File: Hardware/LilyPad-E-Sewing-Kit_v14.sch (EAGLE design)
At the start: 43 parts

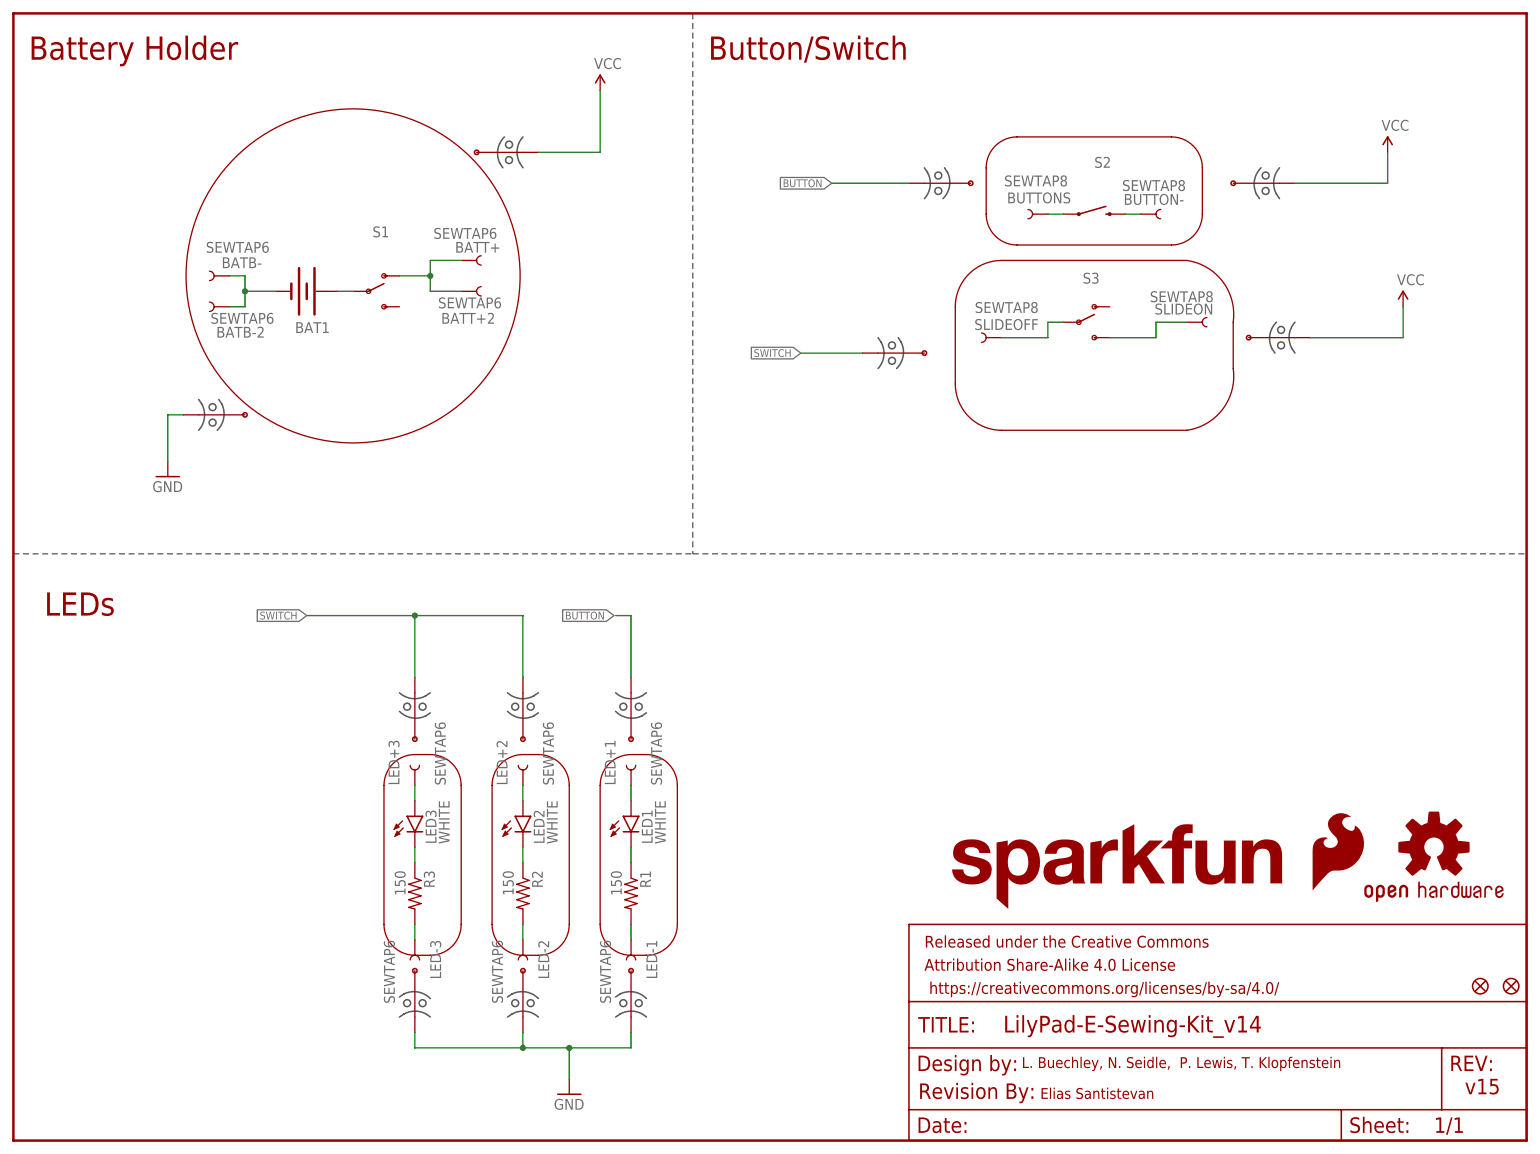
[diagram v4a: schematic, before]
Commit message: Updated schematic
Special Ordering Instructions, two more fiducials, dashed lines to
dilineate parts along with labels amongst other minor changes.
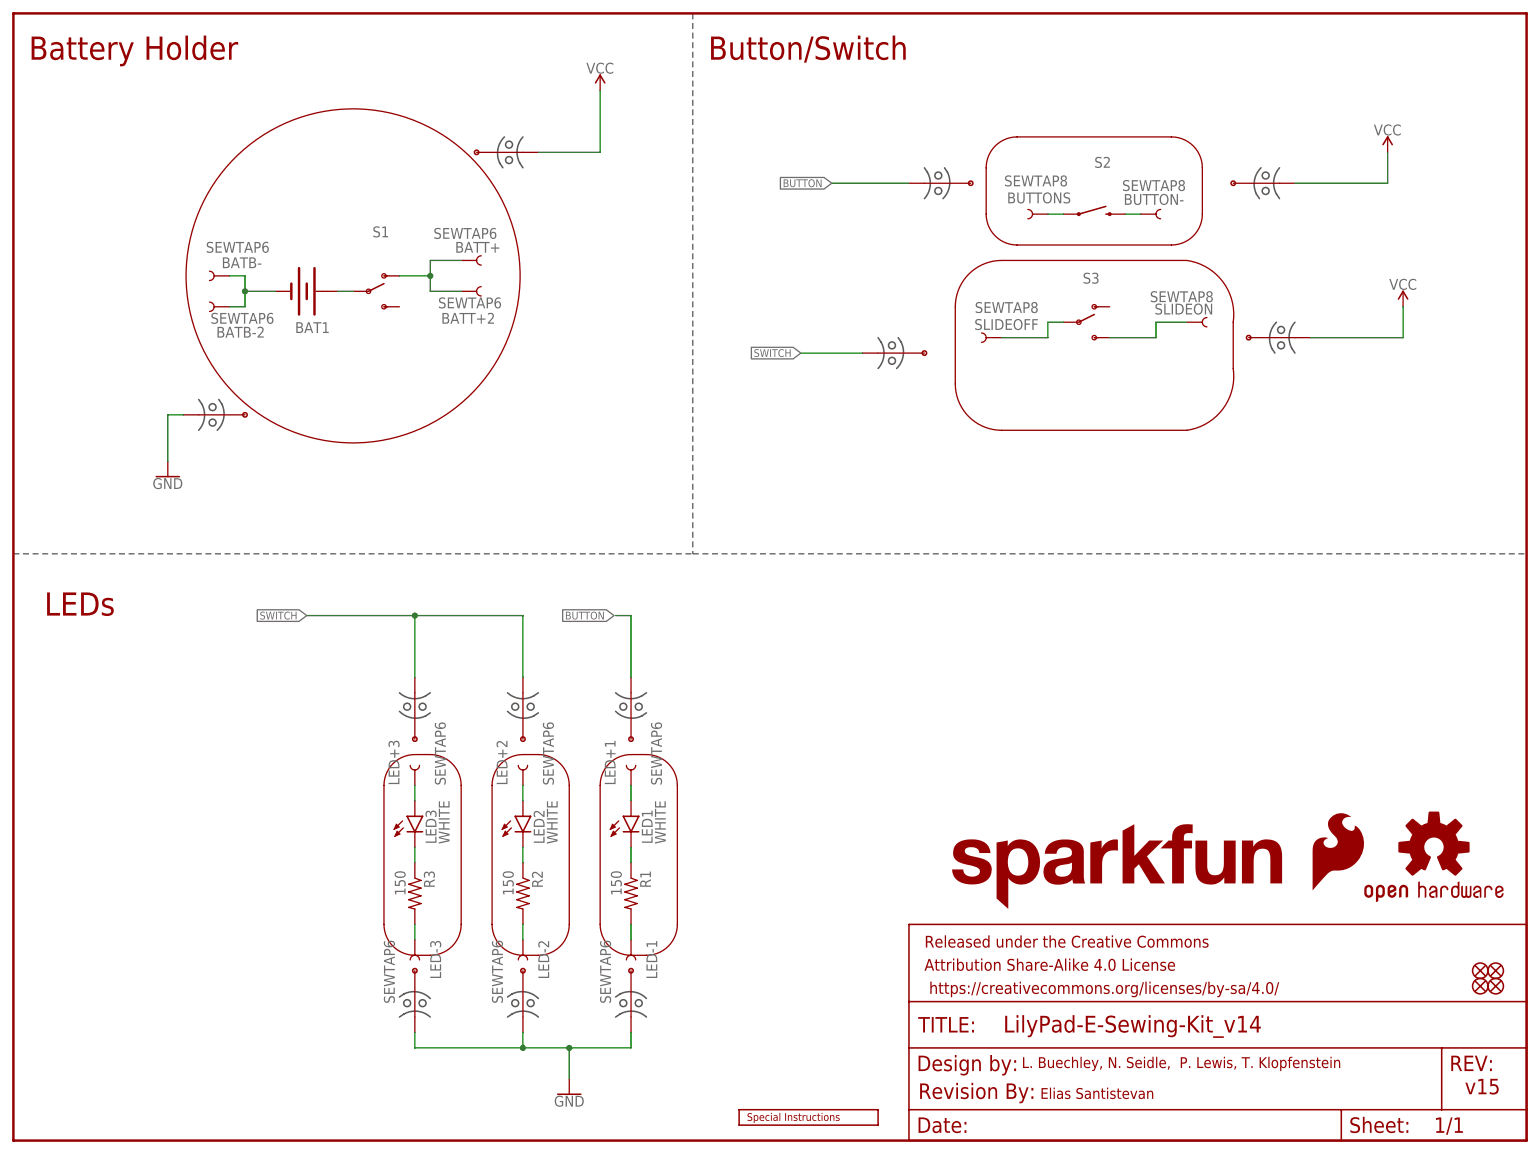
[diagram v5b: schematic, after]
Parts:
- added FD3, FD4: FIDUCIALUFIDUCIAL, SparkFun-Aesthetics:FIDUCIALUFIDUCIAL
- added U$9: SPECIAL_INSTRUCTIONS-ORDERING, SparkFun-Aesthetics:SPECIAL_INSTRUCTIONS-ORDERING
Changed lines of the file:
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@@
 <part name="MB10" library="Testing" deviceset="MOUSE-BITE-1" device="2_HOLES"/>
 <part name="MB1" library="Testing" deviceset="MOUSE-BITE-1" device="2_HOLES"/>
-<part name="GND17" library="SparkFun" deviceset="GND" device=""/>
+<part name="GND17" library="SparkFun-PowerSymbols" deviceset="GND" device=""/>
 <part name="BAT1" library="SparkFun-Electromechanical" deviceset="BATTERY" device="20MM_4LEGS" value="20mm coincell"/>
 <part name="BATB-2" library="LilyPad-Wearables" deviceset="SEWTAP" device="6"/>
@@
 <part name="MB+" library="Testing" deviceset="MOUSE-BITE-1" device="2_HOLES"/>
 <part name="MB-" library="Testing" deviceset="MOUSE-BITE-1" device="2_HOLES"/>
-<part name="GND1" library="SparkFun-Aesthetics" deviceset="GND" device=""/>
-<part name="P+1" library="SparkFun-Aesthetics" deviceset="VCC" device=""/>
-<part name="P+2" library="SparkFun-Aesthetics" deviceset="VCC" device=""/>
-<part name="P+3" library="SparkFun-Aesthetics" deviceset="VCC" device=""/>
+<part name="GND1" library="SparkFun-PowerSymbols" deviceset="GND" device=""/>
+<part name="P+1" library="SparkFun-PowerSymbols" deviceset="VCC" device=""/>
+<part name="P+2" library="SparkFun-PowerSymbols" deviceset="VCC" device=""/>
+<part name="P+3" library="SparkFun-PowerSymbols" deviceset="VCC" device=""/>
 <part name="R3" library="SparkFun-Resistors" deviceset="150OHM-1/10W-1%(0603)" device="" value="150"/>
 <part name="LED+3" library="LilyPad-Wearables" deviceset="SEWTAP" device="6"/>
@@
 <part name="FD2" library="SparkFun-Aesthetics" deviceset="FIDUCIAL" device="UFIDUCIAL"/>
 <part name="LOGO3" library="SparkFun-Aesthetics" deviceset="SFE_LOGO_NAME" device=".1_INCH"/>
+<part name="U$9" library="SparkFun-Aesthetics" deviceset="SPECIAL_INSTRUCTIONS" device="-ORDERING"/>
+<part name="FD3" library="SparkFun-Aesthetics" deviceset="FIDUCIAL" device="UFIDUCIAL"/>
+<part name="FD4" library="SparkFun-Aesthetics" deviceset="FIDUCIAL" device="UFIDUCIAL"/>
 </parts>
 <sheets>
@@
 <instance part="LOGO1" gate="G$1" x="213.36" y="40.64"/>
 <instance part="LOGO2" gate="G$1" x="233.68" y="48.26"/>
-<instance part="FD1" gate="G$1" x="246.38" y="25.4"/>
+<instance part="FD1" gate="G$1" x="243.84" y="25.4"/>
 <instance part="FD2" gate="G$1" x="241.3" y="25.4"/>
 <instance part="LOGO3" gate="G$1" x="152.4" y="38.1"/>
+<instance part="U$9" gate="G$1" x="119.38" y="2.54"/>
+<instance part="FD3" gate="G$1" x="241.3" y="27.94"/>
+<instance part="FD4" gate="G$1" x="243.84" y="27.94"/>
 </instances>
 <busses>

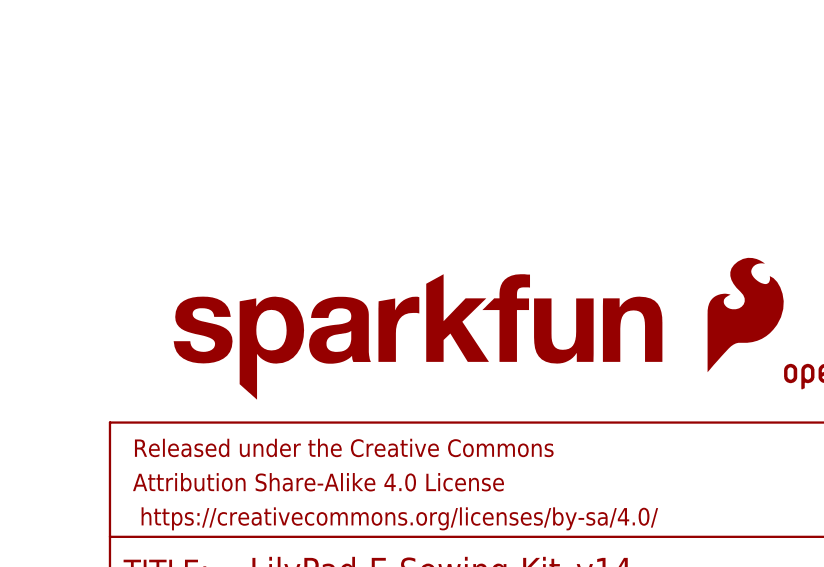
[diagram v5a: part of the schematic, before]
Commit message: Final text object put into place
"E-Sewing Protosnap" was added as silk according to dimension outlines
specified in the Lilypad document provided by Lilypad Coordinator.
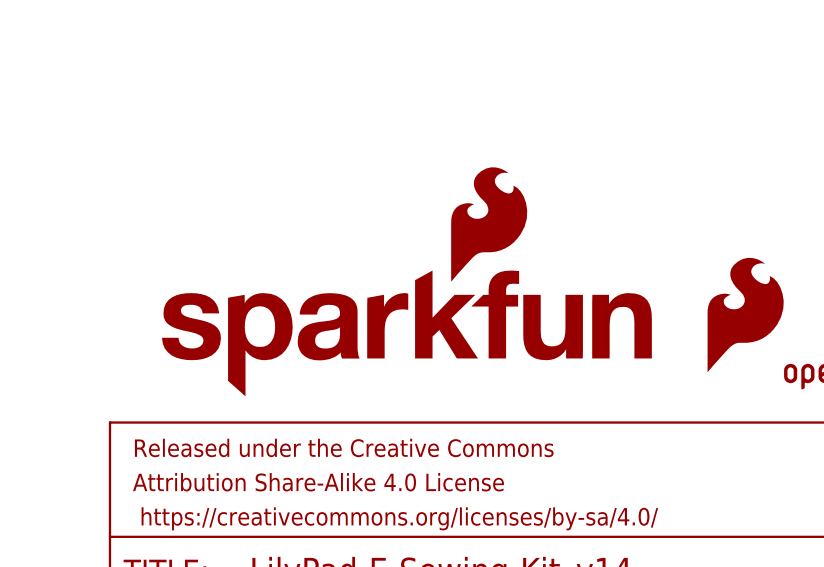
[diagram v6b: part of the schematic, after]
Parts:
- LOGO3: value SFE_LOGO_NAME.1_INCH -> SFE_LOGO_NAME_FLAME.1_INCH; device SparkFun-Aesthetics:SFE_LOGO_NAME.1_INCH -> SparkFun-Aesthetics:SFE_LOGO_NAME_FLAME.1_INCH
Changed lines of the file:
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@@
 <part name="FD1" library="SparkFun-Aesthetics" deviceset="FIDUCIAL" device="UFIDUCIAL"/>
 <part name="FD2" library="SparkFun-Aesthetics" deviceset="FIDUCIAL" device="UFIDUCIAL"/>
-<part name="LOGO3" library="SparkFun-Aesthetics" deviceset="SFE_LOGO_NAME" device=".1_INCH"/>
+<part name="LOGO3" library="SparkFun-Aesthetics" deviceset="SFE_LOGO_NAME_FLAME" device=".1_INCH" value="SFE_LOGO_NAME_FLAME.1_INCH"/>
 <part name="U$9" library="SparkFun-Aesthetics" deviceset="SPECIAL_INSTRUCTIONS" device="-ORDERING"/>
 <part name="FD3" library="SparkFun-Aesthetics" deviceset="FIDUCIAL" device="UFIDUCIAL"/>
@@
 <instance part="LED-2" gate="G$1" x="83.82" y="30.48" rot="R270"/>
 <instance part="LED2" gate="G$1" x="83.82" y="53.34" smashed="yes">
-<attribute name="NAME" x="87.376" y="48.768" size="1.778" layer="95" rot="R90"/>
-<attribute name="VALUE" x="89.535" y="48.768" size="1.778" layer="96" rot="R90"/>
+<attribute name="NAME" x="87.376" y="48.768" size="1.778" layer="95" font="vector" rot="R90"/>
+<attribute name="VALUE" x="89.535" y="48.768" size="1.778" layer="96" font="vector" rot="R90"/>
 </instance>
 <instance part="R1" gate="G$1" x="101.6" y="40.64" rot="R270"/>
@@
 </instance>
 <instance part="BATT+2" gate="G$1" x="76.2" y="139.7" smashed="yes">
-<attribute name="NAME" x="70.358" y="134.366" size="1.778" layer="95"/>
+<attribute name="NAME" x="70.358" y="134.366" size="1.778" layer="95" font="vector"/>
 <attribute name="VALUE" x="69.85" y="136.906" size="1.778" layer="96" font="vector"/>
 </instance>
@@
 </instance>
 <instance part="S2" gate="G$1" x="177.8" y="152.4" smashed="yes">
-<attribute name="NAME" x="177.8" y="160.02" size="1.778" layer="95"/>
+<attribute name="NAME" x="177.8" y="160.02" size="1.778" layer="95" font="vector"/>
 </instance>
 <instance part="S3" gate="1" x="175.26" y="134.62" smashed="yes">
-<attribute name="NAME" x="175.895" y="140.97" size="1.778" layer="95"/>
+<attribute name="NAME" x="175.895" y="140.97" size="1.778" layer="95" font="vector"/>
 </instance>
 <instance part="FRAME1" gate="G$1" x="0" y="0"/>
